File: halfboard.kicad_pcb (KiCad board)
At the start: 2 copper layers, 240.1 x 87.9 mm, 54 parts, among them U1 

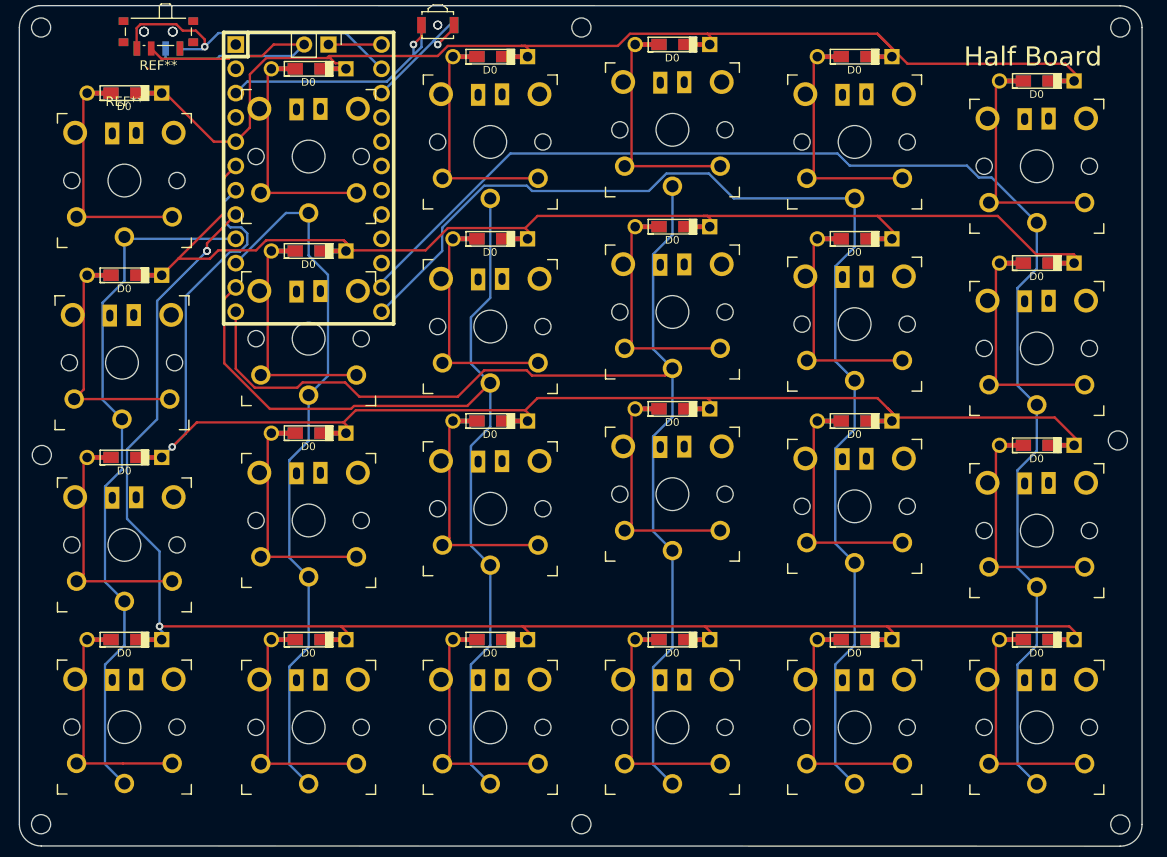
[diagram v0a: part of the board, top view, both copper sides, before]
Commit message: switch to a universal switch footprint. supports mx, alps, choc v1/v2.
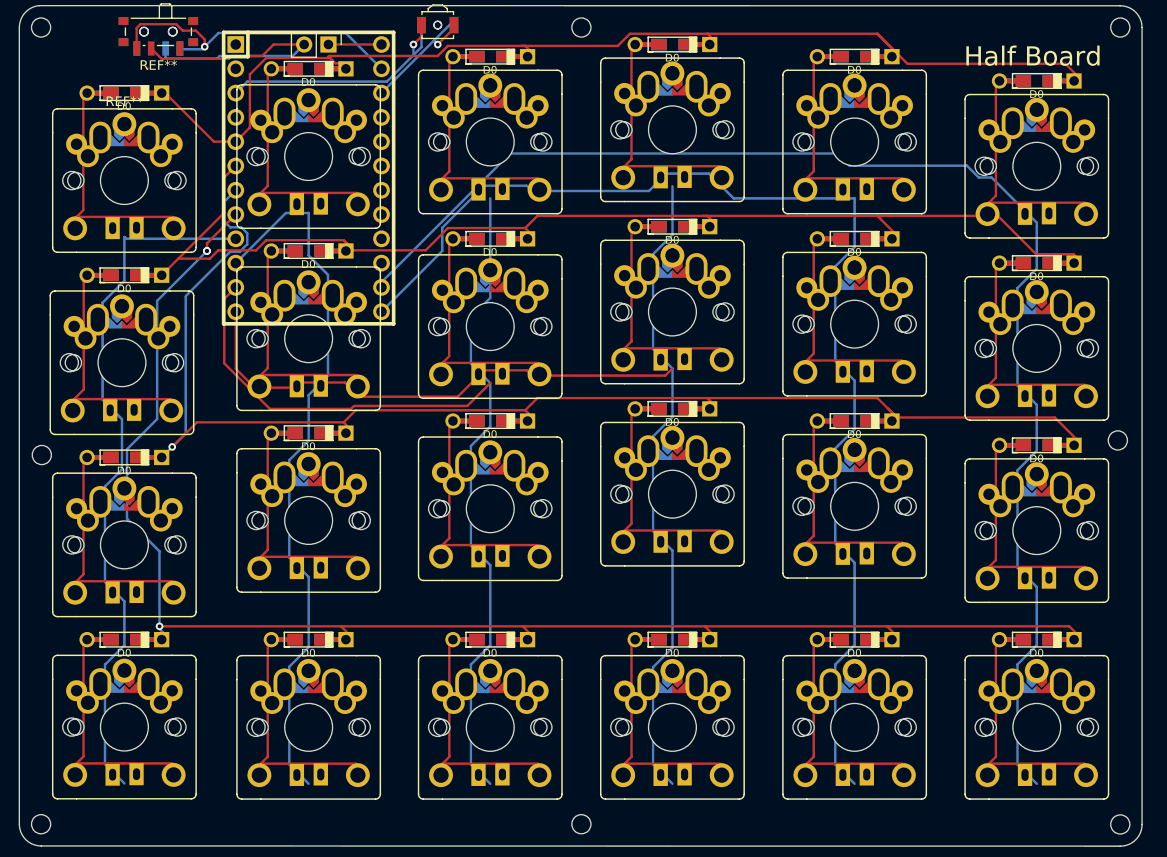
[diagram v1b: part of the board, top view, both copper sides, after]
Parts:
- removed the   at (144.4, 62.3)
- removed the   at (125.4, 59.7)
- removed the   at (106.3, 58.4)
- removed the   at (106.3, 77.5)
- removed the   at (106.3, 96.5)
- removed the   at (87.3, 98.1)
- removed the   at (87.3, 79.0)
- removed the   at (87.3, 59.7)
- removed the   at (68.3, 61.2)
- removed the   at (68.3, 80.3)
- removed the   at (68.3, 99.3)
- removed the   at (144.4, 81.3)
- removed the   at (68.3, 120.9)
- removed the   at (49.0, 120.9)
- removed the   at (49.0, 101.9)
- removed the   at (144.4, 100.4)
- removed the   at (144.4, 120.9)
- removed the   at (125.4, 120.9)
- removed the   at (106.3, 120.9)
- removed the   at (87.3, 120.9)
- removed the   at (125.4, 97.8)
- removed the   at (125.4, 78.8)
- removed the REF** at (52.6, 48.5) (x2)
- added  : , halfboard:MX-ALPs-PG1350-LED-FLIP, F.Cu at (144.4, 62.3)
- added  : , halfboard:MX-ALPs-PG1350-LED-FLIP, F.Cu at (125.4, 59.7)
- added  : , halfboard:MX-ALPs-PG1350-LED-FLIP, F.Cu at (106.3, 58.4)
- added  : , halfboard:MX-ALPs-PG1350-LED-FLIP, F.Cu at (106.3, 77.5)
- added  : , halfboard:MX-ALPs-PG1350-LED-FLIP, F.Cu at (106.3, 96.5)
- added  : , halfboard:MX-ALPs-PG1350-LED-FLIP, F.Cu at (87.3, 98.1)
- added  : , halfboard:MX-ALPs-PG1350-LED-FLIP, F.Cu at (87.3, 79.0)
- added  : , halfboard:MX-ALPs-PG1350-LED-FLIP, F.Cu at (87.3, 59.7)
- added  : , halfboard:MX-ALPs-PG1350-LED-FLIP, F.Cu at (68.3, 61.2)
- added  : , halfboard:MX-ALPs-PG1350-LED-FLIP, F.Cu at (68.3, 80.3)
- added  : , halfboard:MX-ALPs-PG1350-LED-FLIP, F.Cu at (68.3, 99.3)
- added  : , halfboard:MX-ALPs-PG1350-LED-FLIP, F.Cu at (144.4, 81.3)
- added  : , halfboard:MX-ALPs-PG1350-LED-FLIP, F.Cu at (68.3, 120.9)
- added  : , halfboard:MX-ALPs-PG1350-LED-FLIP, F.Cu at (49.0, 120.9)
- added  : , halfboard:MX-ALPs-PG1350-LED-FLIP, F.Cu at (49.0, 101.9)
- added  : , halfboard:MX-ALPs-PG1350-LED-FLIP, F.Cu at (144.4, 100.4)
- added  : , halfboard:MX-ALPs-PG1350-LED-FLIP, F.Cu at (144.4, 120.9)
- added  : , halfboard:MX-ALPs-PG1350-LED-FLIP, F.Cu at (125.4, 120.9)
- added  : , halfboard:MX-ALPs-PG1350-LED-FLIP, F.Cu at (106.3, 120.9)
- added  : , halfboard:MX-ALPs-PG1350-LED-FLIP, F.Cu at (87.3, 120.9)
- added  : , halfboard:MX-ALPs-PG1350-LED-FLIP, F.Cu at (125.4, 97.8)
- added  : , halfboard:MX-ALPs-PG1350-LED-FLIP, F.Cu at (125.4, 78.8)
- added REF**: SW_SPDT_PCM12, Button_Switch_SMD:SW_SPDT_PCM12, F.Cu at (52.6, 48.5)
- added REF**: SW_SPDT_PCM12, Button_Switch_SMD:SW_SPDT_PCM12, B.Cu at (52.6, 48.5)
-  : footprint halfboard:SW_PG1350_reversible -> halfboard:MX-ALPs-PG1350-LED-FLIP
- REF**: value SW_PG1350_reversible -> MX/ALPs/PG1350; footprint halfboard:SW_PG1350_reversible -> halfboard:MX-ALPs-PG1350-LED-FLIP

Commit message: clean footprint
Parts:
- removed the REF** at (52.6, 48.5) (x2)
- added REF**: SW_SPDT_PCM12, Button_Switch_SMD:SW_SPDT_PCM12, F.Cu at (52.6, 48.5)
- added REF**: SW_SPDT_PCM12, Button_Switch_SMD:SW_SPDT_PCM12, B.Cu at (52.6, 48.5)
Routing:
- net col2: track 105.6 -> 39.3 mm
- net (no net): track 0.00 -> 66.2 mm

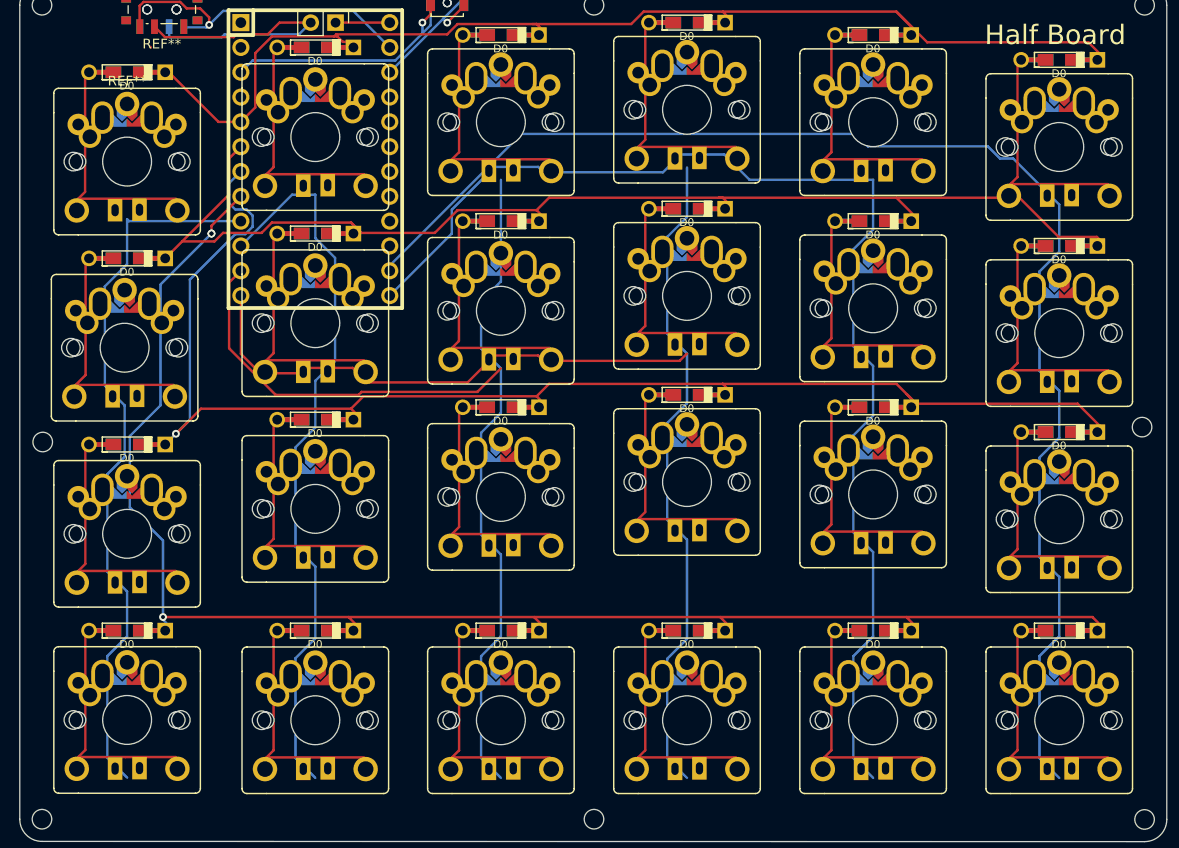
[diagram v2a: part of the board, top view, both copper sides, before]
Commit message: tweak universal footprint a bit more
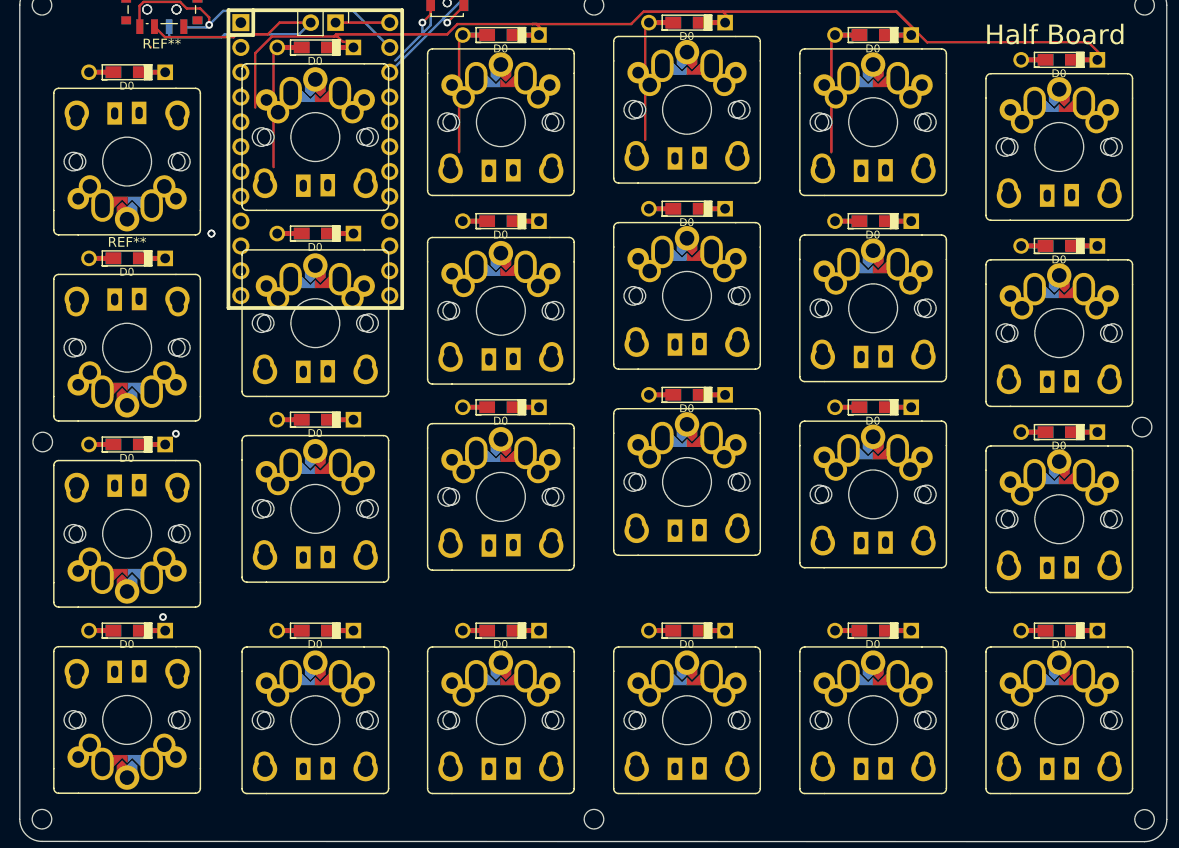
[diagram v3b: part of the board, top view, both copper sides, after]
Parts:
- removed the REF** at (52.6, 48.5) (x2)
- added REF**: SW_SPDT_PCM12, Button_Switch_SMD:SW_SPDT_PCM12, F.Cu at (52.6, 48.5)
- added REF**: SW_SPDT_PCM12, Button_Switch_SMD:SW_SPDT_PCM12, B.Cu at (52.6, 48.5)
- moved   0.25 mm to (49.0, 82.8), turned to 180 degrees
- turned   to 180 degrees (x2)
- turned REF** to 180 degrees
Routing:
- net row3: track 155.2 -> 0.00 mm
- net col5: track 141.3 -> 0.00 mm
- net row2: track 139.2 -> 0.00 mm
- net col4: track 124.7 -> 0.00 mm
- net col3: track 122.5 -> 0.00 mm
- net row1: track 121.3 -> 0.00 mm
- net col1: track 74.5 -> 0.00 mm
- net col0: track 73.9 -> 0.00 mm
- net (no net): track 66.2 -> 0.00 mm
- net col2: track 39.3 -> 0.00 mm
- net col0_row1: track 23.4 -> 0.00 mm
- net col2_row1: track 23.3 -> 0.00 mm
- net col1_row3: track 23.3 -> 0.00 mm
- net col4_row3: track 23.3 -> 0.00 mm
- net col3_row3: track 23.3 -> 0.00 mm
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
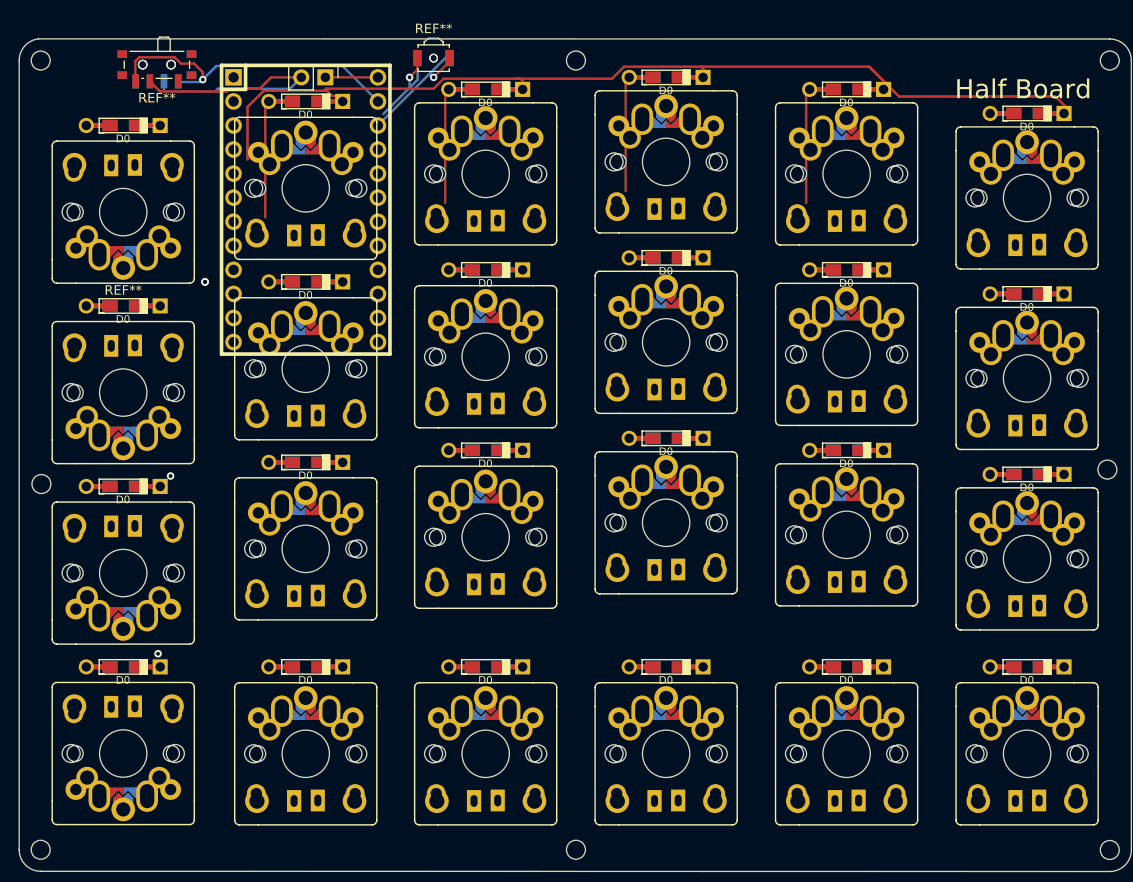
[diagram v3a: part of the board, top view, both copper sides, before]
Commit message: route traces and fix spacing of footprints
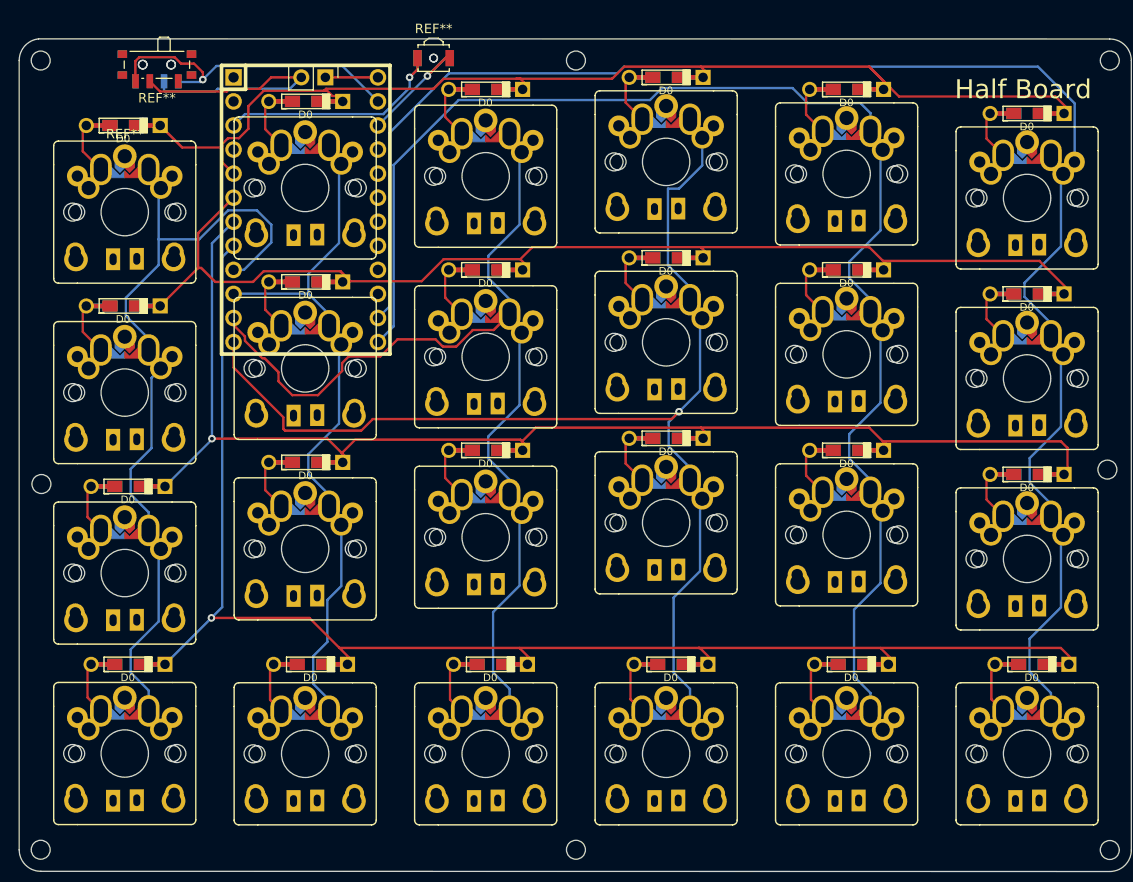
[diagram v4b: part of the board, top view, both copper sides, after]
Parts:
- removed the   at (87.3, 59.7)
- removed the   at (68.3, 61.2)
- removed the   at (68.3, 80.3)
- removed the   at (68.3, 99.3)
- removed the   at (68.3, 120.9)
- removed the   at (49.0, 120.9)
- removed the   at (49.0, 101.9)
- removed the D0 at (68.3, 111.8)
- removed the D0 at (49.0, 111.8)
- removed the D0 at (49.0, 92.7)
- removed the D0 at (144.4, 111.8)
- removed the D0 at (125.4, 111.8)
- removed the D0 at (106.3, 111.8)
- removed the D0 at (87.3, 111.8)
- removed the REF** at (52.6, 48.5) (x2)
- added  : , halfboard:MX-ALPs-PG1350-LED-FLIP, F.Cu at (87.3, 60.0)
- added  : , halfboard:MX-ALPs-PG1350-LED-FLIP, F.Cu at (68.2, 61.2)
- added  : , halfboard:MX-ALPs-PG1350-LED-FLIP, F.Cu at (68.2, 80.3)
- added  : , halfboard:MX-ALPs-PG1350-LED-FLIP, F.Cu at (68.2, 99.3)
- added  : , halfboard:MX-ALPs-PG1350-LED-FLIP, F.Cu at (68.2, 120.9)
- added  : , halfboard:MX-ALPs-PG1350-LED-FLIP, F.Cu at (49.2, 120.9)
- added  : , halfboard:MX-ALPs-PG1350-LED-FLIP, F.Cu at (49.2, 101.9)
- added D0: D, mlp:Diode-dual, F.Cu at (68.8, 111.5)
- added D0: D, mlp:Diode-dual, F.Cu at (49.5, 111.5)
- added D0: D, mlp:Diode-dual, F.Cu at (49.5, 92.7)
- added D0: D, mlp:Diode-dual, F.Cu at (144.9, 111.5)
- added D0: D, mlp:Diode-dual, F.Cu at (125.9, 111.5)
- added D0: D, mlp:Diode-dual, F.Cu at (106.8, 111.5)
- added D0: D, mlp:Diode-dual, F.Cu at (87.8, 111.5)
- added REF**: SW_SPDT_PCM12, Button_Switch_SMD:SW_SPDT_PCM12, F.Cu at (52.6, 48.5)
- added REF**: SW_SPDT_PCM12, Button_Switch_SMD:SW_SPDT_PCM12, B.Cu at (52.6, 48.5)
- moved   0.16 mm to (49.2, 82.8), turned to 0 degrees
- moved REF** 0.16 mm to (49.2, 63.8), turned to 0 degrees
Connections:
- REF** pad 1: (no net) -> col0
- REF** pad 2: (no net) -> col0_row0
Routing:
- net col5: track 0.00 -> 163.5 mm
- net row3: track 0.00 -> 150.3 mm, vias 3 -> 1
- net col4: track 0.00 -> 138.2 mm
- net row2: track 0.00 -> 131.5 mm
- net col3: track 0.00 -> 118.1 mm, vias 0 -> 1
- net row1: track 0.00 -> 116.9 mm
- net col2: track 0.00 -> 100.3 mm
- net col0: track 0.00 -> 78.9 mm
- net col1: track 0.00 -> 68.4 mm
- net RESET_GND: track 11.5 -> 26.1 mm
- net row0: track 107.7 -> 118.8 mm
- net col3_row0: track 13.0 -> 5.66 mm
- net col1_row0: track 12.2 -> 5.34 mm
- net col4_row0: track 12.0 -> 5.15 mm
- net col2_row0: track 12.5 -> 5.91 mm
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
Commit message: various tweaks
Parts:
- removed the REF** at (52.6, 48.5) (x2)
- added REF**: SW_SPDT_PCM12, Button_Switch_SMD:SW_SPDT_PCM12, F.Cu at (52.6, 48.5)
- added REF**: SW_SPDT_PCM12, Button_Switch_SMD:SW_SPDT_PCM12, B.Cu at (52.6, 48.5)
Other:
- board size 240.1 x 87.9 mm -> 117.4 x 87.9 mm
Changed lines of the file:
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@@
   (general
     (thickness 1.6)
-    (drawings 42)
+    (drawings 18)
     (tracks 385)
     (zones 0)
@@
     (38 B.Mask user)
     (39 F.Mask user)
-    (40 Dwgs.User user hide)
-    (41 Cmts.User user hide)
+    (40 Dwgs.User user)
+    (41 Cmts.User user)
     (42 Eco1.User user)
-    (43 Eco2.User user hide)
+    (43 Eco2.User user)
     (44 Edge.Cuts user)
     (45 Margin user)
@@
     (pad_to_mask_clearance 0)
     (aux_axis_origin 0 0)
-    (visible_elements FFFFFFFF)
+    (visible_elements FFFFE7FF)
     (pcbplotparams
       (layerselection 0x3ffff_ffffffff)
@@
     )
   )
-  (gr_line (start 181.61 80.01) (end 186.055 80.01) (layer Edge.Cuts) (width 0.05))
-  (gr_arc (start 191.135 77.47) (end 186.055 80.01) (angle -126.8698976) (layer Edge.Cuts) (width 0.05))
-  (gr_circle (center 219.49 47.752) (end 220.49 47.752) (layer Edge.Cuts) (width 0.05))
-  (gr_arc (start 202.946042 47.752) (end 202.692043 45.48011) (angle -83.70000491) (layer Edge.Cuts) (width 0.05))
-  (gr_line (start 275.83002 45.48011) (end 202.692043 45.48011) (layer Edge.Cuts) (width 0.05))
-  (gr_arc (start 179.338067 47.752) (end 181.61 47.752) (angle -90.40000105) (layer Edge.Cuts) (width 0.05))
-  (gr_line (start 200.66 80.01) (end 200.66 47.755161) (layer Edge.Cuts) (width 0.05))
-  (gr_line (start 196.215 80.01) (end 200.66 80.01) (layer Edge.Cuts) (width 0.05))
-  (gr_line (start 181.61 47.752) (end 181.61 80.01) (layer Edge.Cuts) (width 0.05))
-  (gr_circle (center 275.59 90.932) (end 276.59 90.932) (layer Edge.Cuts) (width 0.05))
-  (gr_line (start 163.007795 133.33391) (end 275.832054 133.358666) (layer Edge.Cuts) (width 0.05))
-  (gr_line (start 278.117967 131.086777) (end 278.115933 47.751999) (layer Edge.Cuts) (width 0.05))
-  (gr_line (start 179.322206 45.480122) (end 162.766068 45.466002) (layer Edge.Cuts) (width 0.05))
-  (gr_line (start 160.72 47.752001) (end 160.72 131.062033) (layer Edge.Cuts) (width 0.05))
-  (gr_arc (start 163.020067 47.752001) (end 162.766068 45.466002) (angle -83.65983026) (layer Edge.Cuts) (width 0.05))
-  (gr_arc (start 275.844 47.752) (end 278.115933 47.751999) (angle -90.35253802) (layer Edge.Cuts) (width 0.05))
-  (gr_arc (start 275.846034 131.086776) (end 278.117967 131.086777) (angle 90.35253802) (layer Edge.Cuts) (width 0.05))
-  (gr_arc (start 162.991933 131.062032) (end 160.72 131.062033) (angle -90.4) (layer Edge.Cuts) (width 0.05))
-  (gr_circle (center 275.844 47.752) (end 276.844 47.752) (layer Edge.Cuts) (width 0.05))
-  (gr_circle (center 162.991933 47.752001) (end 163.991933 47.752001) (layer Edge.Cuts) (width 0.05))
-  (gr_circle (center 163.068 92.456) (end 164.068 92.456) (layer Edge.Cuts) (width 0.05))
-  (gr_circle (center 219.491426 131.062032) (end 220.491426 131.062032) (layer Edge.Cuts) (width 0.05))
-  (gr_circle (center 275.844 131.086776) (end 276.844 131.086776) (layer Edge.Cuts) (width 0.05))
-  (gr_circle (center 162.991933 131.062032) (end 163.991933 131.062032) (layer Edge.Cuts) (width 0.05))
   (gr_circle (center 40.309933 131.062032) (end 41.309933 131.062032) (layer Edge.Cuts) (width 0.05))
   (gr_circle (center 153.162 131.086776) (end 154.162 131.086776) (layer Edge.Cuts) (width 0.05))
